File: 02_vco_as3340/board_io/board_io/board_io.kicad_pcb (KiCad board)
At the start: 2 copper layers, 70 x 40 mm, 14 parts, among them J1 Tuning RVs, J12 Mode Switch, J13 Power, J15 SYNC MODE, J2 PWM offset, J3 FM CV LVL, J4 PWM CV LVL, SW2 SW_SPDT

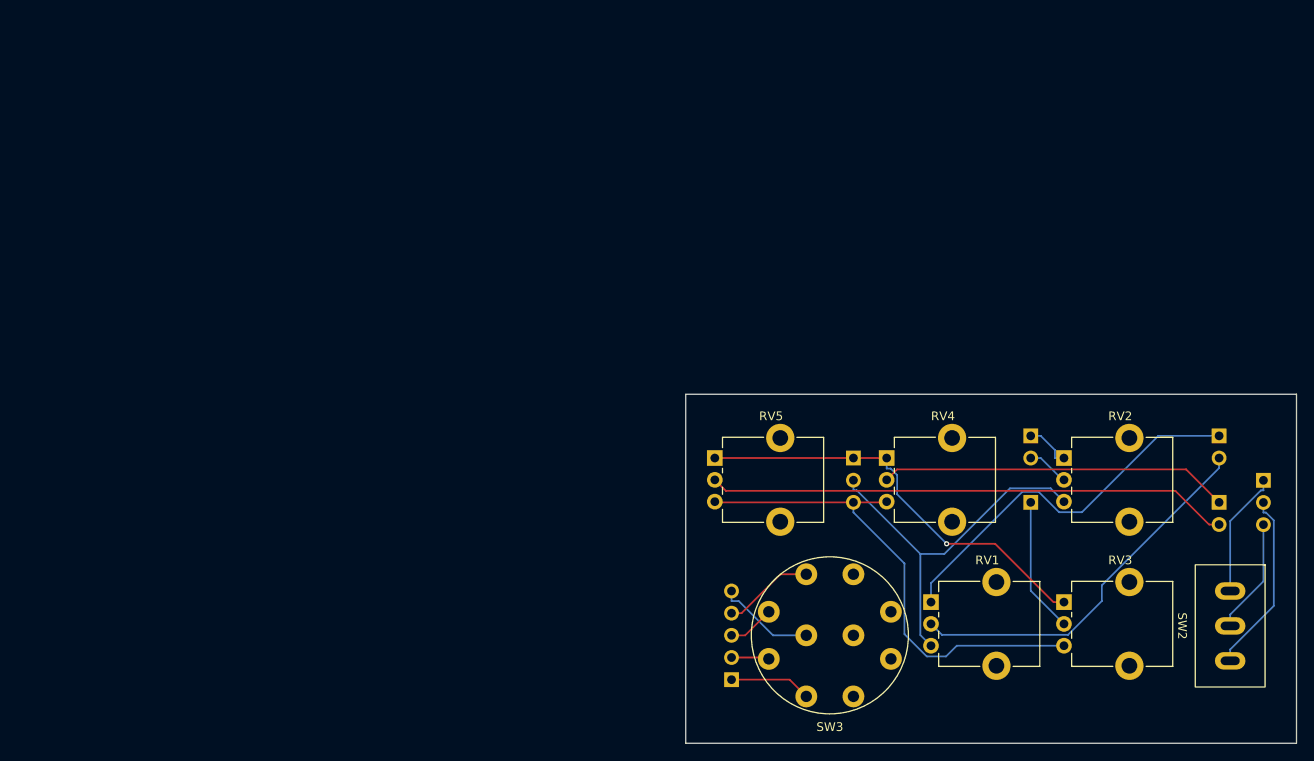
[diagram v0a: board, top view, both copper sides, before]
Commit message: made sub board for 02
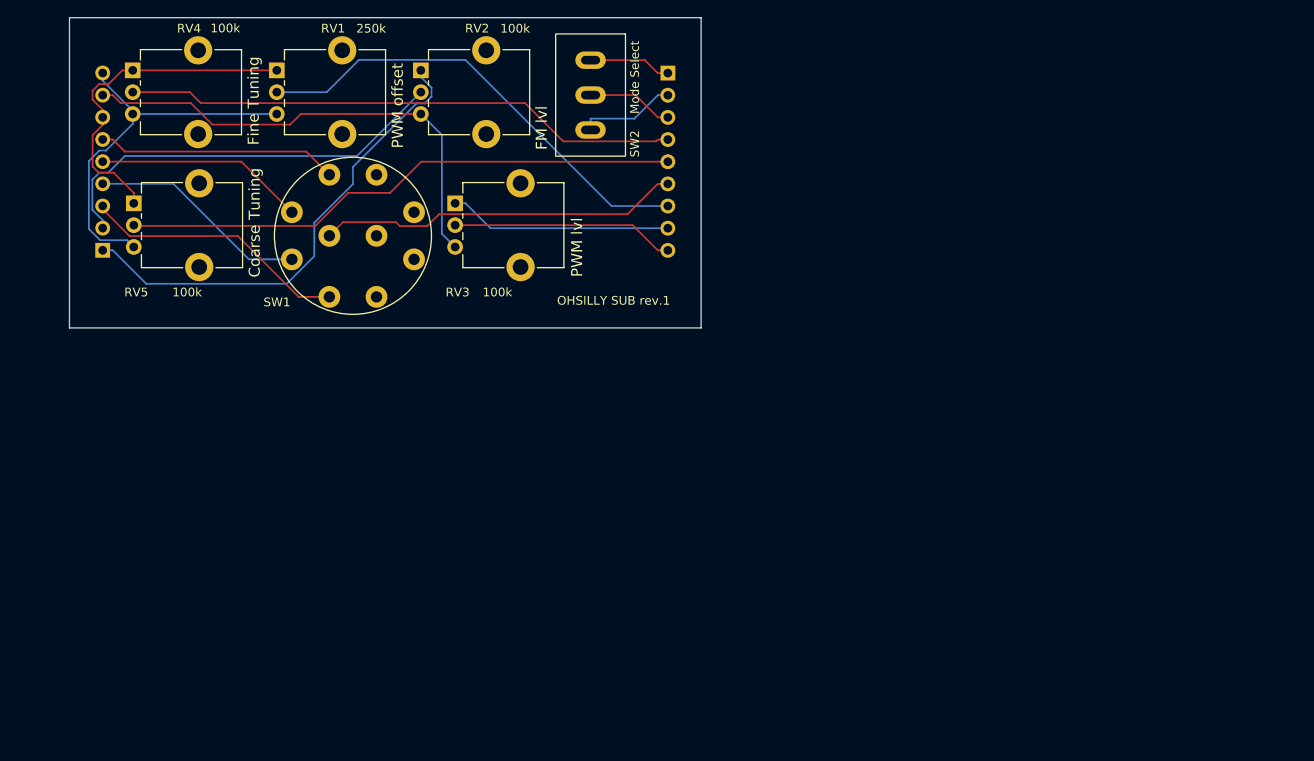
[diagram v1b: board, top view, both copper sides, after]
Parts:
- removed J12: Mode Switch, Connector_PinHeader_2.54mm:PinHeader_1x03_P2.54mm_Vertical
- removed J13: Power, Connector_PinHeader_2.54mm:PinHeader_1x03_P2.54mm_Vertical
- removed J15: SYNC MODE, Connector_PinHeader_2.54mm:PinHeader_1x05_P2.54mm_Vertical
- removed J3: FM CV LVL, Connector_PinHeader_2.54mm:PinHeader_1x02_P2.54mm_Vertical
- removed J4: PWM CV LVL, Connector_PinHeader_2.54mm:PinHeader_1x02_P2.54mm_Vertical
- removed SW3: ~, cynthia:mini rotary switch
- added SW1: ~, cynthia:mini rotary switch, F.Cu at (51.9, 41.8)
- J1: value Tuning RVs -> Header 1; footprint Connector_PinHeader_2.54mm:PinHeader_1x02_P2.54mm_Vertical -> Connector_PinHeader_2.54mm:PinHeader_1x09_P2.54mm_Vertical
- J2: value PWM offset -> Header 2; footprint Connector_PinHeader_2.54mm:PinHeader_1x01_P2.54mm_Vertical -> Connector_PinHeader_2.54mm:PinHeader_1x09_P2.54mm_Vertical
- RV1: value 100k -> 250k
- RV3: value 250k -> 100k
- moved J1 131.2 mm to (23.2, 43.5), turned to 0 degrees
- moved RV4 97.2 mm to (26.6, 22.9)
- moved RV1 96.6 mm to (43.1, 22.9)
- moved SW2 95.3 mm to (79.1, 25.7)
- moved RV2 86.1 mm to (59.6, 22.9)
- moved RV3 83.4 mm to (63.6, 38.1)
- moved RV5 72.7 mm to (26.7, 38.1)
- moved J2 64.4 mm to (88.0, 23.2)
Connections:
- J1 pad 1: Net-(J1-Pin_1) -> FM CV Hot
- J1 pad 2: Net-(J1-Pin_2) -> FM CV Levelled
- J2 pad 1: Net-(J2-Pin_1) -> Mode LFO
- RV1 pad 1: Net-(J4-Pin_1) -> +12V
- RV1 pad 2: Net-(J4-Pin_2) -> PWM Offset
- RV1 pad 3: GND -> -12V
- RV2 pad 1: Net-(J3-Pin_1) -> FM CV Hot
- RV2 pad 2: Net-(J3-Pin_2) -> FM CV Levelled
- RV3 pad 1: +12V -> PWM CV Hot
- RV3 pad 2: Net-(J2-Pin_1) -> PWM CV Levelled
- RV3 pad 3: -12V -> GND
- RV4 pad 2: Net-(J1-Pin_1) -> Fine Tuning
- RV5 pad 2: Net-(J1-Pin_2) -> Coarse Tuning
- SW2 pad 1: Net-(J12-Pin_1) -> Mode LFO
- SW2 pad 2: Net-(J12-Pin_3) -> Mode COM
- SW2 pad 3: Net-(J12-Pin_2) -> Mode VCO
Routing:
- net Coarse Tuning: track 0.00 -> 64.3 mm
- net Fine Tuning: track 0.00 -> 63.7 mm
- net Net-(J1-Pin_2): track 59.9 -> 0.00 mm
- net FM CV Hot: track 0.00 -> 55.1 mm
- net PWM Offset: track 0.00 -> 53.3 mm
- net FM CV Levelled: track 0.00 -> 47.8 mm
- net Net-(J4-Pin_1): track 44.1 -> 0.00 mm
- net Net-(J4-Pin_2): track 43.7 -> 0.00 mm
- net Sync COM: track 0.00 -> 41.6 mm
- net Net-(J1-Pin_1): track 40.2 -> 0.00 mm
- net Hard Sync +: track 0.00 -> 30.5 mm
- net Soft Sync: track 0.00 -> 27.7 mm
- net PWM CV Levelled: track 0.00 -> 25.6 mm
- net PWM CV Hot: track 0.00 -> 25.6 mm
- net Hard Sync: track 0.00 -> 25.3 mm
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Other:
- board size 70 x 40 mm -> 72.4 x 35.6 mm
- board text added: "OHSILLY SUB rev.1"

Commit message: routed everyting
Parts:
- removed J1: Header 1, Connector_PinHeader_2.54mm:PinHeader_1x09_P2.54mm_Vertical
- removed J2: Header 2, Connector_PinHeader_2.54mm:PinHeader_1x09_P2.54mm_Vertical
- added J3: Header 1, Connector_PinHeader_2.54mm:PinHeader_2x05_P2.54mm_Vertical, B.Cu at (32.4, 49.3)
- added J4: Header 2, Connector_PinHeader_2.54mm:PinHeader_2x04_P2.54mm_Vertical, B.Cu at (64.4, 21.8)
- moved RV2 52.2 mm to (19.0, 55.6)
- moved RV5 32.9 mm to (54.6, 55.6)
- moved RV4 32.4 mm to (54.6, 39.1)
- moved RV3 32.0 mm to (36.8, 55.6)
- moved SW2 29.4 mm to (49.7, 25.5), turned to 0 degrees
- moved SW1 28.5 mm to (24.9, 32.6), turned to -90 degrees
- moved RV1 17.4 mm to (36.8, 39.1)
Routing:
- net Fine Tuning: track 63.7 -> 19.8 mm
- net FM CV Hot: track 55.1 -> 16.2 mm
- net Coarse Tuning: track 64.3 -> 36.9 mm
- net FM CV Levelled: track 47.8 -> 22.3 mm
- net Sync COM: track 41.6 -> 18.2 mm
- net PWM CV Levelled: track 25.6 -> 48.8 mm
- net GND: track 55.2 -> 32.6 mm
- net PWM CV Hot: track 25.6 -> 44.2 mm
- net PWM Offset: track 53.3 -> 37.0 mm
- net Hard Sync +: track 30.5 -> 18.7 mm
- net +12V: track 38.9 -> 49.1 mm
- net Mode LFO: track 9.47 -> 17.8 mm
- net Soft Sync: track 27.7 -> 22.5 mm
- net Mode COM: track 9.92 -> 13.3 mm
- net -12V: track 44.3 -> 47.6 mm
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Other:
- board size 72.4 x 35.6 mm -> 54.5 x 48.2 mm

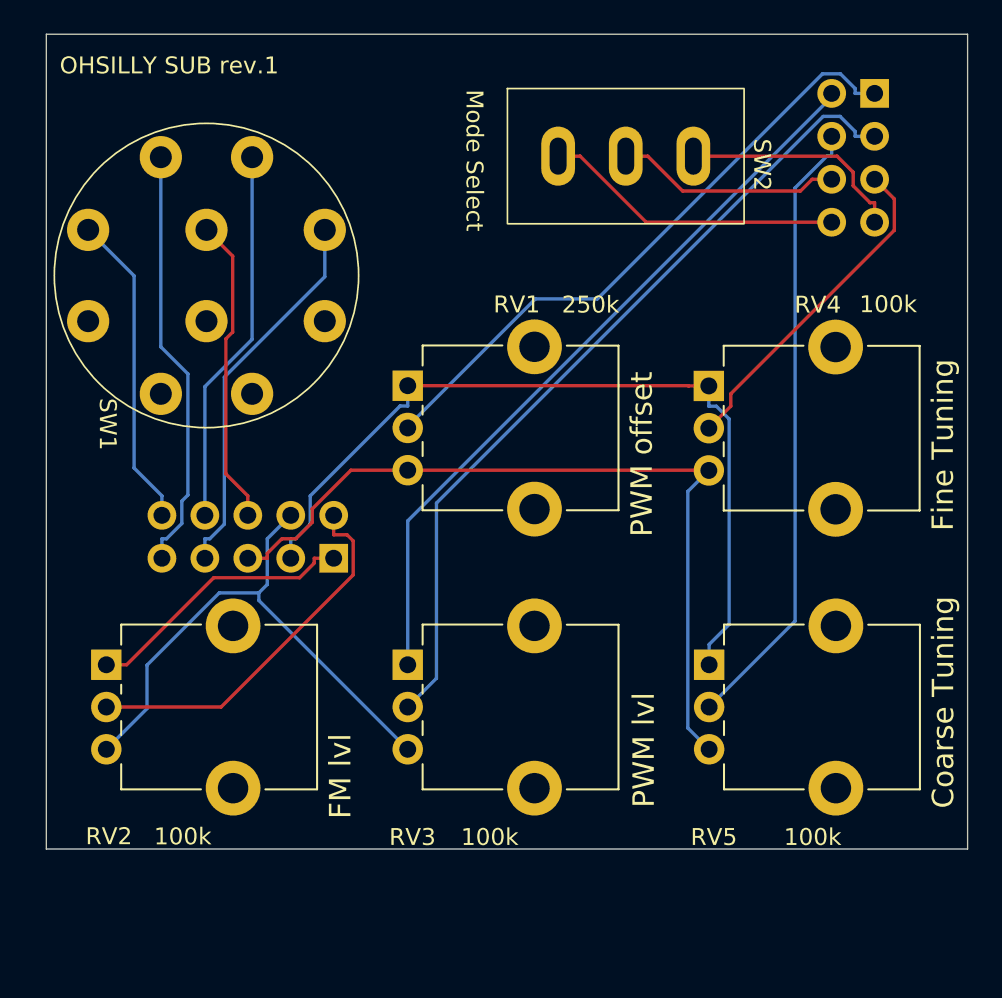
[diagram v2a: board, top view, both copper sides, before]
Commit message: fixed layout front/back
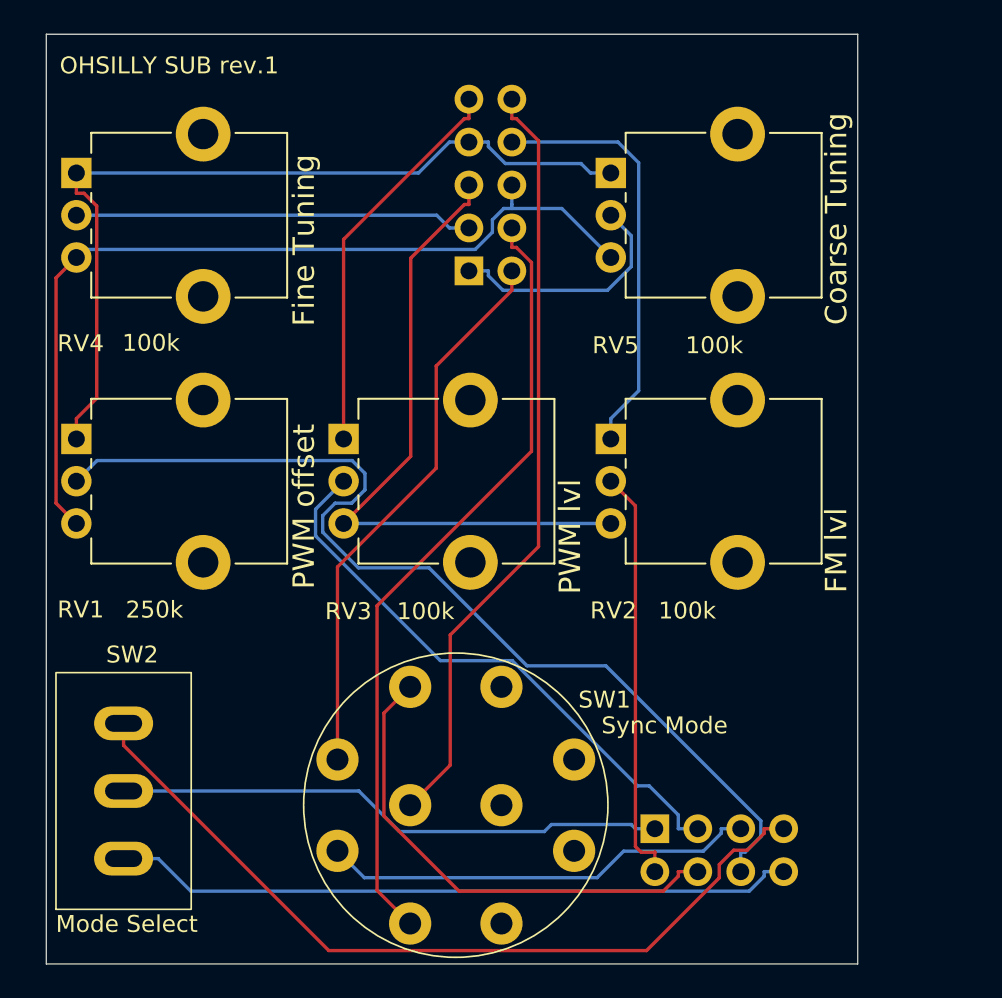
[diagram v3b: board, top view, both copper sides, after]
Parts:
- removed J3: Header 1, Connector_PinHeader_2.54mm:PinHeader_2x05_P2.54mm_Vertical
- removed J4: Header 2, Connector_PinHeader_2.54mm:PinHeader_2x04_P2.54mm_Vertical
- added J1: Header 1, Connector_PinHeader_2.54mm:PinHeader_2x05_P2.54mm_Vertical, B.Cu at (40.4, 32.3)
- added J2: Header 2, Connector_PinHeader_2.54mm:PinHeader_2x04_P2.54mm_Vertical, B.Cu at (51.4, 65.3)
- moved SW2 47.9 mm to (20.0, 63.1), turned to 90 degrees
- moved RV4 39.5 mm to (17.2, 26.5)
- moved SW1 34.6 mm to (39.7, 63.9), turned to 0 degrees
- moved RV2 32.7 mm to (48.8, 42.3)
- moved RV5 29.7 mm to (48.8, 26.5)
- moved RV1 19.9 mm to (17.2, 42.3)
- moved RV3 13.9 mm to (33.0, 42.3)
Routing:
- net Mode VCO: track 13.5 -> 49.0 mm
- net Hard Sync +: track 18.7 -> 46.4 mm
- net Sync COM: track 18.2 -> 45.7 mm
- net Mode LFO: track 17.8 -> 40.5 mm
- net PWM Offset: track 37.0 -> 59.6 mm
- net Coarse Tuning: track 36.9 -> 14.4 mm
- net PWM CV Hot: track 44.2 -> 23.3 mm
- net Mode COM: track 13.3 -> 32.7 mm
- net PWM CV Levelled: track 48.8 -> 34.2 mm
- net Hard Sync -: track 22.3 -> 33.2 mm
- net FM CV Hot: track 16.2 -> 25.0 mm
- net Soft Sync: track 22.5 -> 29.3 mm
- net GND: track 32.6 -> 39.1 mm
- net -12V: track 47.6 -> 52.6 mm
- net Fine Tuning: track 19.8 -> 23.5 mm
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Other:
- board size 54.5 x 48.2 mm -> 48 x 55 mm

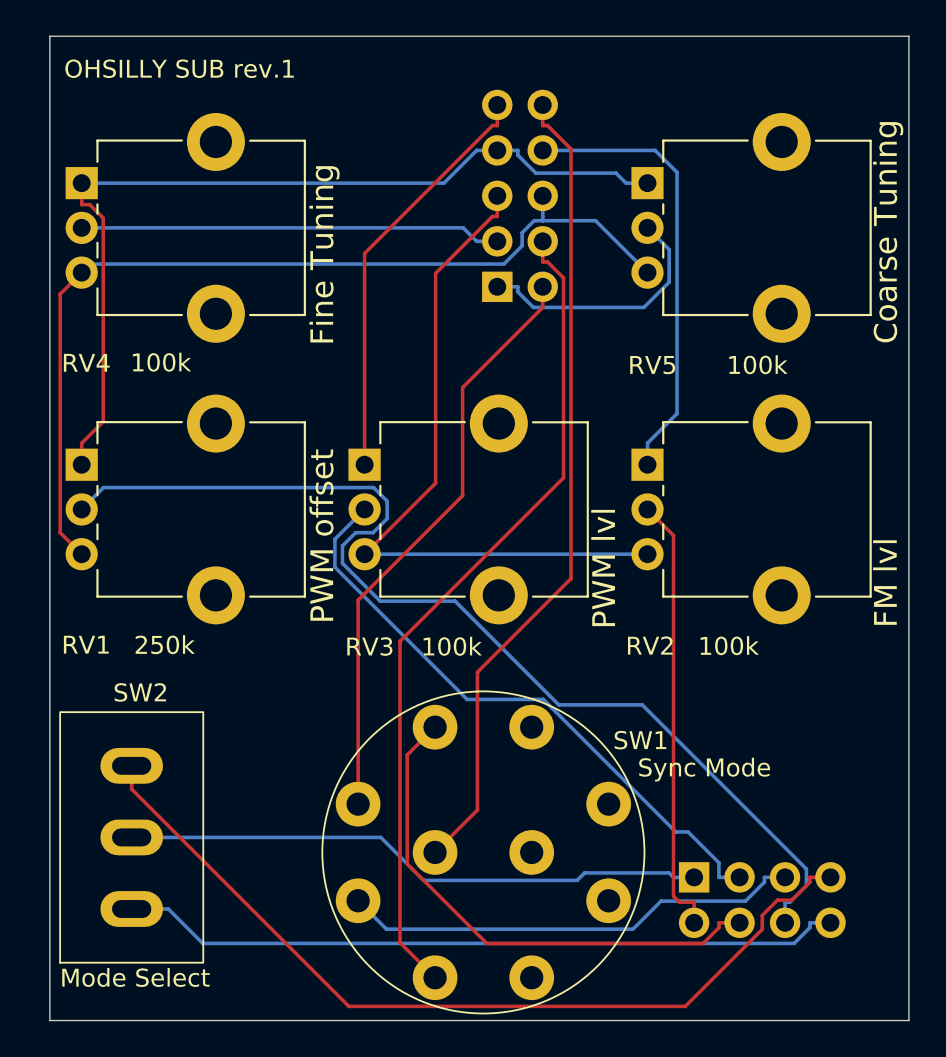
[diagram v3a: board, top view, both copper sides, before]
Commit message: fine-tuned PCB hole distanes
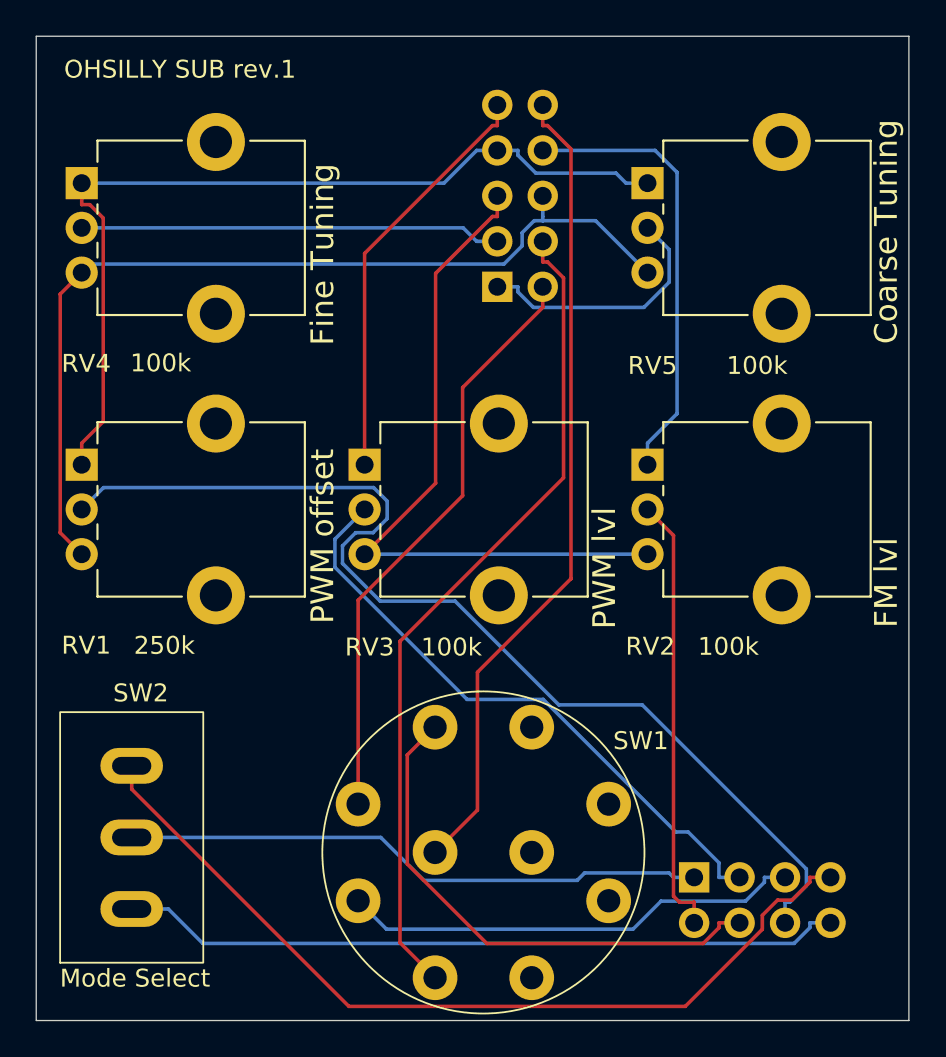
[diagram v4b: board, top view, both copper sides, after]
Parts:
- J1: value Header 1 -> Conn_02x05_Odd_Even
- J2: value Header 2 -> Conn_02x04_Odd_Even
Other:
- board size 48 x 55 mm -> 48.8 x 55 mm
